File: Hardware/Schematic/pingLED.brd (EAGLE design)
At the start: 100 x 80 mm, 10 parts, among them IC1 LM1117MPX-3.3, U1 V_IN

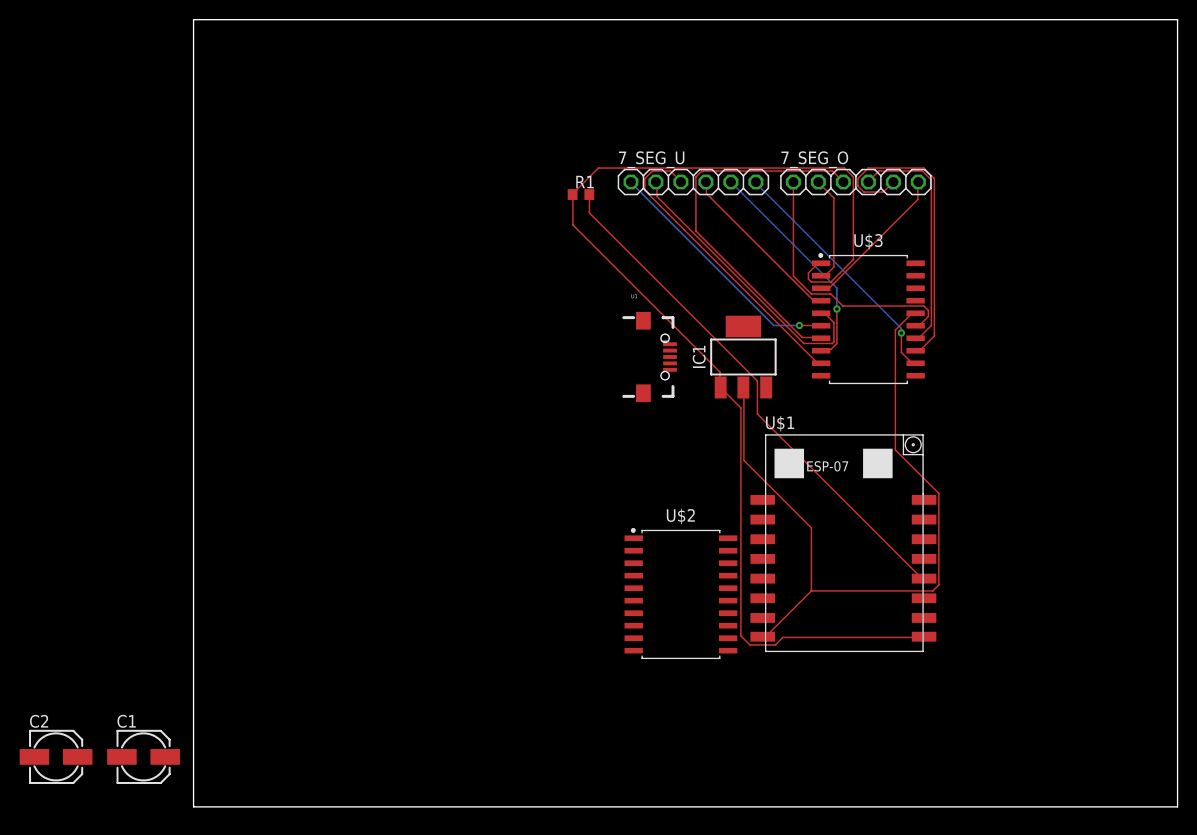
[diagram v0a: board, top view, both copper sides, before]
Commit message: Second hardware revision done. New schematic and layout file. Cleaned up repository.
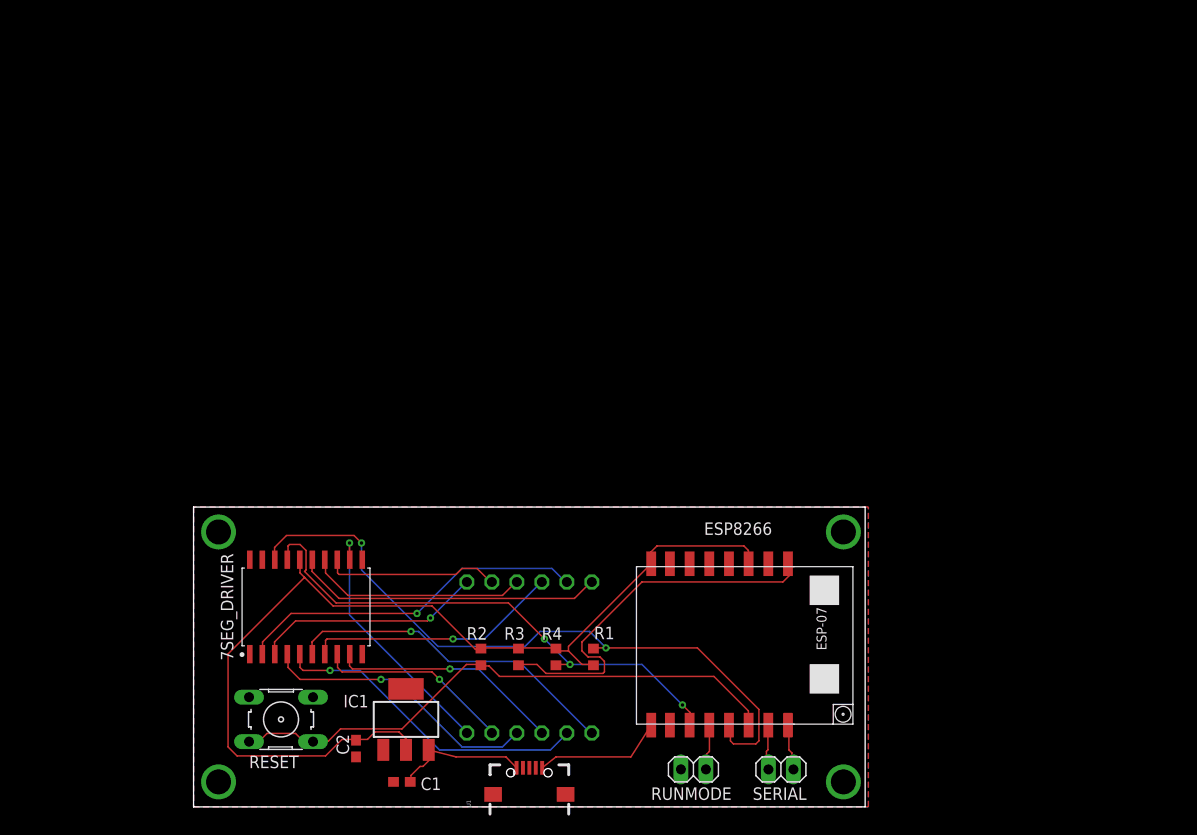
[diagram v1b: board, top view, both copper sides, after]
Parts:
- removed U$1: ESP07-16PIN, esp8266:ESP07-16PIN
- removed U$2, U$3: TM1637SOP20, esp8266:SOIC127P1045X255-20
- added 7SEG_DRIVER: TM1637SOP20, esp8266:SOIC127P1045X255-20
- added ESP8266: ESP07-16PIN, esp8266:ESP07-16PIN
- added H1, H2, H3, H4: SPECIAL_DRILL_0.1000, special-drill:PAD_0.1000
- added R2, R3, R4: (no value), rcl:R0603
- added RESET: (no value), switch-omron:B3F-10XX
- added RUNMODE, SERIAL: (no value), pinhead:1X02
- C1, C2: device rcl:153CLV-0505 -> rcl:C0603
- R1: value 0 -> (none)
- moved 7_SEG_U 58.4 mm to (34.1, 7.51), flipped to the bottom
- moved 7_SEG_O 52.5 mm to (34.1, 22.9), flipped to the bottom
- moved IC1 50.3 mm to (21.6, 8.89)
- moved R1 47.0 mm to (40.6, 15.2), turned to 270 degrees
- moved U1 45.9 mm to (34.1, 1.27), turned to 90 degrees
- moved C2 30.5 mm to (16.5, 5.93), turned to 270 degrees
- moved C1 26.4 mm to (21.2, 2.54), turned to 180 degrees
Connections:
- new net I2C_CLK: 7SEG_DRIVER.18, ESP8266.GPIO5, R1.1
- new net I2C_DIO: 7SEG_DRIVER.17, ESP8266.GPIO2, R4.1
- new net N$2: ESP8266.GPIO4, R2.1, RESET.3, RESET.4
- new net N$3: ESP8266.REST, R3.1
- new net RX: ESP8266.RX, SERIAL.2
- new net TX: ESP8266.TX, SERIAL.1
- net COM_0: now also 7SEG_DRIVER.15; no longer U$3.15
- net COM_1: now also 7SEG_DRIVER.14; no longer U$3.14
- net COM_2: now also 7SEG_DRIVER.13; no longer U$3.13
- net COM_3: now also 7SEG_DRIVER.12; no longer U$3.12
- net GND: now also 7SEG_DRIVER.1, C1.2, C2.2, ESP8266.GND, ESP8266.GPIO15, H1.1, H2.1, H3.1, H4.1, RESET.2, RUNMODE.2; no longer C1.-, C2.-, R1.1, U$1.GND, U$3.1
- net N$1: now also ESP8266.GPIO0, RUNMODE.1; no longer R1.2, U$1.GPIO0
- net N$4: now also C1.1; no longer C1.+
- net SEG_A: now also 7SEG_DRIVER.2; no longer U$3.2
- net SEG_B: now also 7SEG_DRIVER.3; no longer U$3.3
- net SEG_C: now also 7SEG_DRIVER.4; no longer U$3.4
- net SEG_D: now also 7SEG_DRIVER.5; no longer U$3.5
- net SEG_DP: now also 7SEG_DRIVER.9; no longer U$3.9
- net SEG_E: now also 7SEG_DRIVER.6; no longer U$3.6
- net SEG_F: now also 7SEG_DRIVER.7; no longer U$3.7
- net SEG_G: now also 7SEG_DRIVER.8; no longer U$3.8
- net VCC: now also 7SEG_DRIVER.16, C2.1, ESP8266.CH_PD, ESP8266.VCC, R1.2, R2.2, R3.2, R4.2; no longer C2.+, U$1.VCC, U$3.16
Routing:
- net GND: track 117.7 -> 13.2 mm
- net I2C_CLK: track 0.00 -> 70.5 mm, vias 0 -> 2
- net N$2: track 0.00 -> 58.1 mm
- net I2C_DIO: track 0.00 -> 53.7 mm, vias 0 -> 3
- net N$1: track 53.3 -> 4.68 mm
- net N$3: track 0.00 -> 39.1 mm
- net VCC: track 74.1 -> 101.9 mm
- net SEG_A: track 11.0 -> 35.8 mm, vias 0 -> 1
- net COM_2: track 32.2 -> 17.9 mm
- net N$4: track 0.00 -> 13.7 mm
- net SEG_F: track 38.4 -> 25.9 mm, vias 0 -> 1
- net SEG_C: track 17.4 -> 28.5 mm, vias 0 -> 1
- net SEG_E: track 25.4 -> 34.4 mm
- net SEG_B: track 15.3 -> 23.3 mm, vias 0 -> 1
- net SEG_DP: track 30.9 -> 23.6 mm, vias 0 -> 1
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- added copper zone on layer 1, net GND
- added copper zone on layer 16, net GND
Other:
- board size 100 x 80 mm -> 68.2 x 30.5 mm
- board text added: "PingLED v2 Jonas Heim 03.2019"
- board text added: "RX"
- board text added: "TX"
